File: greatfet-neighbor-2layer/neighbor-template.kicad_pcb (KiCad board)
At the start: 2 copper layers, 70.7 x 53.3 mm, 13 parts, among them J1 NEIGHBOR1, J2 NEIGHBOR2, J7 BONUS_ROW, U1 M24C02-FMN6TP

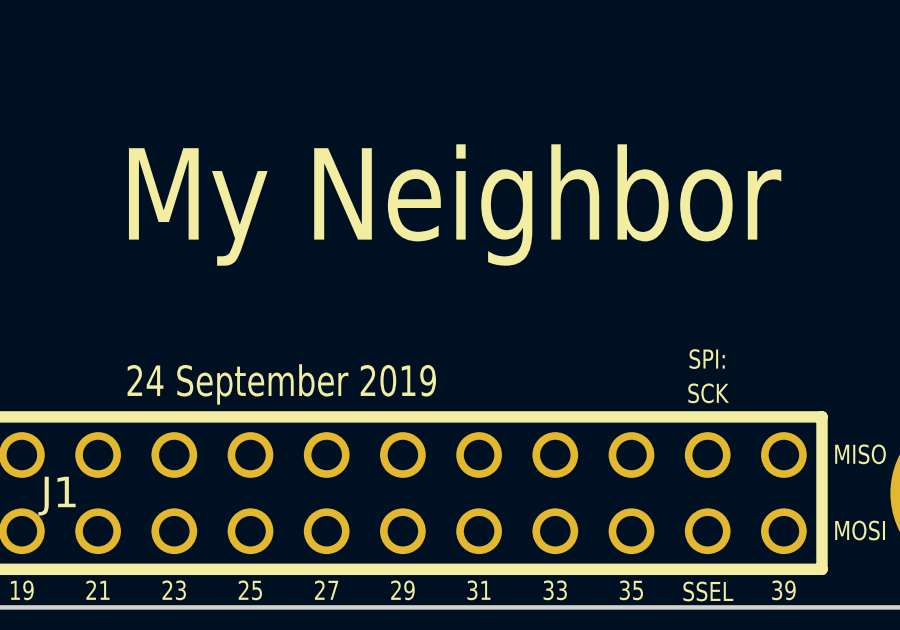
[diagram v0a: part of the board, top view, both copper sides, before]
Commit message: add "for GreatFET" to schematic, silkscreen add template README
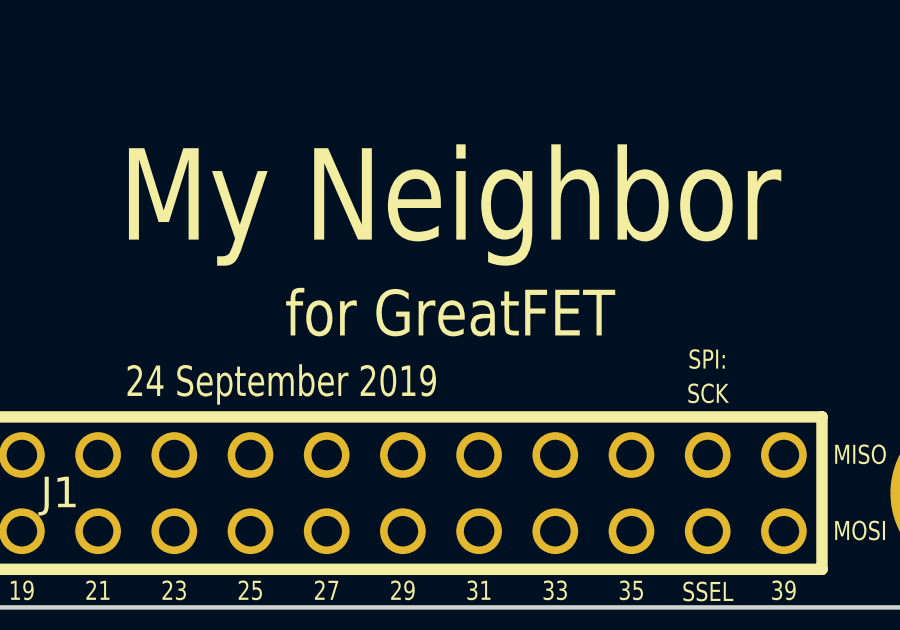
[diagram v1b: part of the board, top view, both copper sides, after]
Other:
- board text added: "for GreatFET"
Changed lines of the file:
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@@
   (general
     (thickness 1.6)
-    (drawings 234)
+    (drawings 235)
     (tracks 75)
     (zones 0)
@@
   )
   (setup
-    (last_trace_width 0.3048)
+    (last_trace_width 0.2032)
     (user_trace_width 0.3048)
     (user_trace_width 0.508)
@@
       (net 1 GND))
   )
+  (gr_text "for GreatFET" (at 159.05 112.15) (layer F.SilkS)
+    (effects (font (size 1.524 1.27) (thickness 0.2286)))
+  )
   (gr_line (start 109.6772 98.933) (end 109.728 99.9998) (angle 90) (layer Edge.Cuts) (width 0.15))

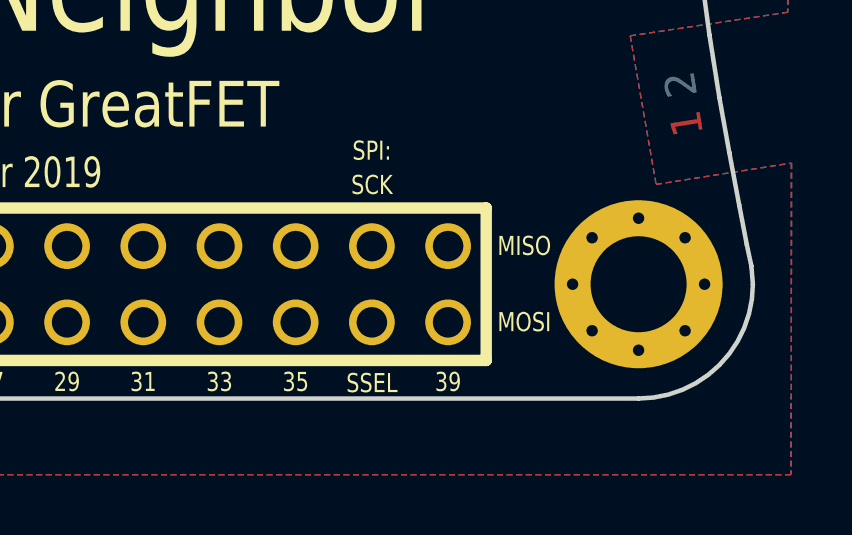
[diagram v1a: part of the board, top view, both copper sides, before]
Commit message: adopt OSHWA convention for SPI signal names https://www.oshwa.org/a-resolution-to-redefine-spi-signal-names
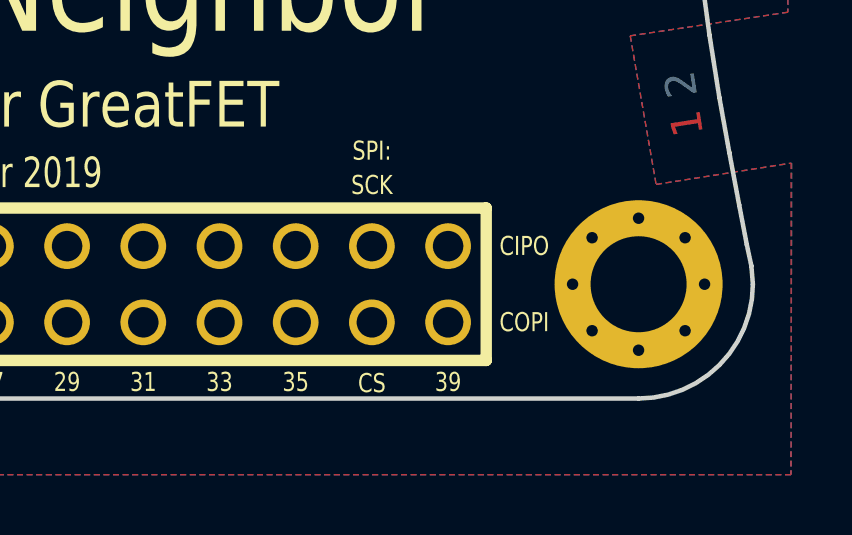
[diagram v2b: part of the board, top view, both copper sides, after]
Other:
- board text added: "CIPO"
- board text added: "COPI"
- board text added: "CS"
- board text removed: "MISO"
- board text removed: "MOSI"
- board text removed: "SSEL"
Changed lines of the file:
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@@
     (effects (font (size 0.635 0.508) (thickness 0.1016)) (justify mirror))
   )
-  (gr_text MOSI (at 172.72 119.38) (layer B.SilkS)
-    (effects (font (size 0.635 0.508) (thickness 0.1016)) (justify mirror))
-  )
-  (gr_text MISO (at 172.72 116.84) (layer B.SilkS)
+  (gr_text COPI (at 172.72 119.38) (layer B.SilkS)
+    (effects (font (size 0.635 0.508) (thickness 0.1016)) (justify mirror))
+  )
+  (gr_text CIPO (at 172.72 116.84) (layer B.SilkS)
     (effects (font (size 0.635 0.508) (thickness 0.1016)) (justify mirror))
   )
@@
     (effects (font (size 0.635 0.508) (thickness 0.1016)) (justify mirror))
   )
-  (gr_text SSEL (at 167.64 121.412) (layer B.SilkS)
+  (gr_text CS (at 167.64 121.412) (layer B.SilkS)
     (effects (font (size 0.635 0.508) (thickness 0.1016)) (justify mirror))
   )
@@
     (effects (font (size 0.635 0.508) (thickness 0.1016)))
   )
-  (gr_text SSEL (at 167.64 121.412) (layer F.SilkS)
-    (effects (font (size 0.635 0.508) (thickness 0.1016)))
-  )
-  (gr_text MISO (at 172.72 116.84) (layer F.SilkS)
-    (effects (font (size 0.635 0.508) (thickness 0.1016)))
-  )
-  (gr_text MOSI (at 172.72 119.38) (layer F.SilkS)
-    (effects (font (size 0.635 0.508) (thickness 0.1016)))
-  )
+  (gr_text CS (at 167.64 121.412) (layer F.SilkS)
+    (effects (font (size 0.635 0.508) (thickness 0.1016)))
+  )
+  (gr_text CIPO (at 172.72 116.84) (layer F.SilkS)
+    (effects (font (size 0.635 0.508) (thickness 0.1016)))
+  )
+  (gr_text COPI (at 172.72 119.38) (layer F.SilkS)
+    (effects (font (size 0.635 0.508) (thickness 0.1016)))
+  )
